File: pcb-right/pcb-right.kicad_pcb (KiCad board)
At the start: 2 copper layers, 84 parts, among them SW1 SW_Push, U1 ATmega32U4-AU, Y1 16MHz

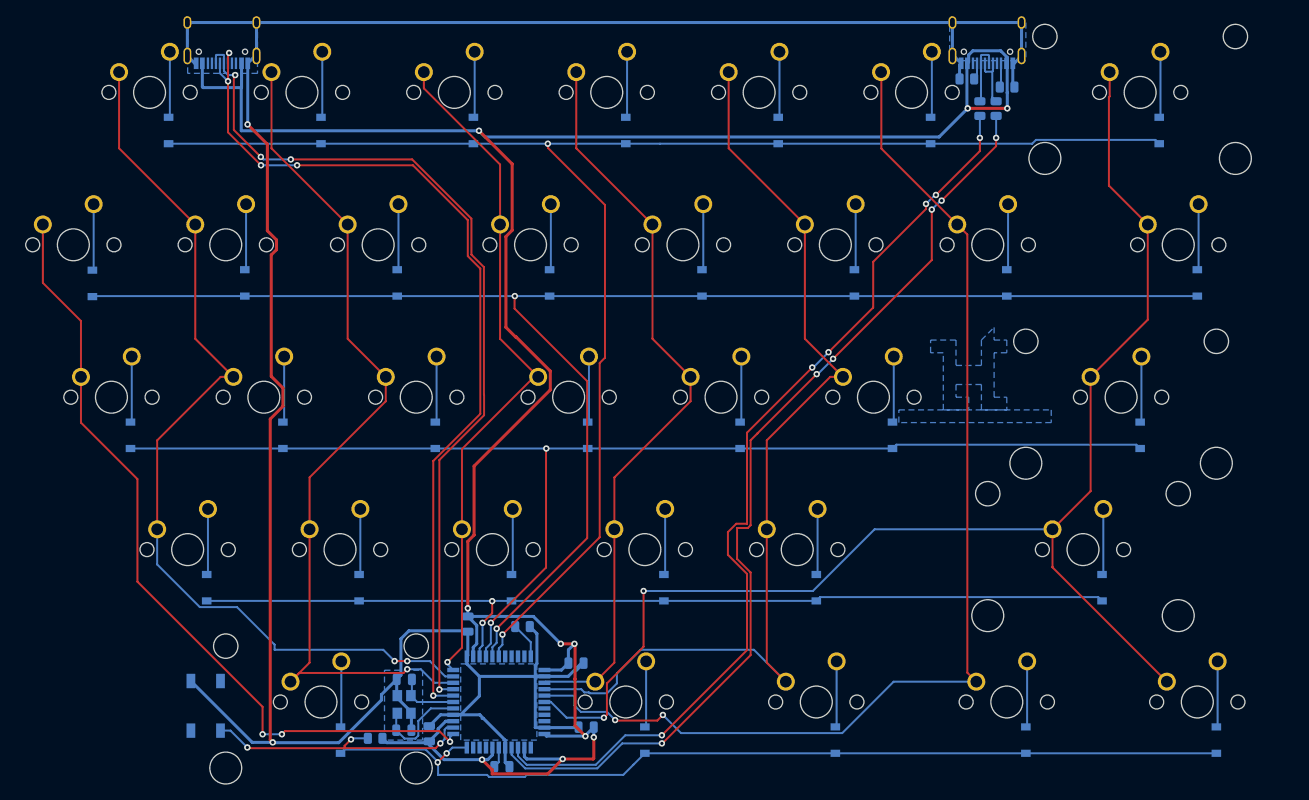
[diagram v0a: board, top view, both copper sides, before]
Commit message: added files for manufacturing right side pcb
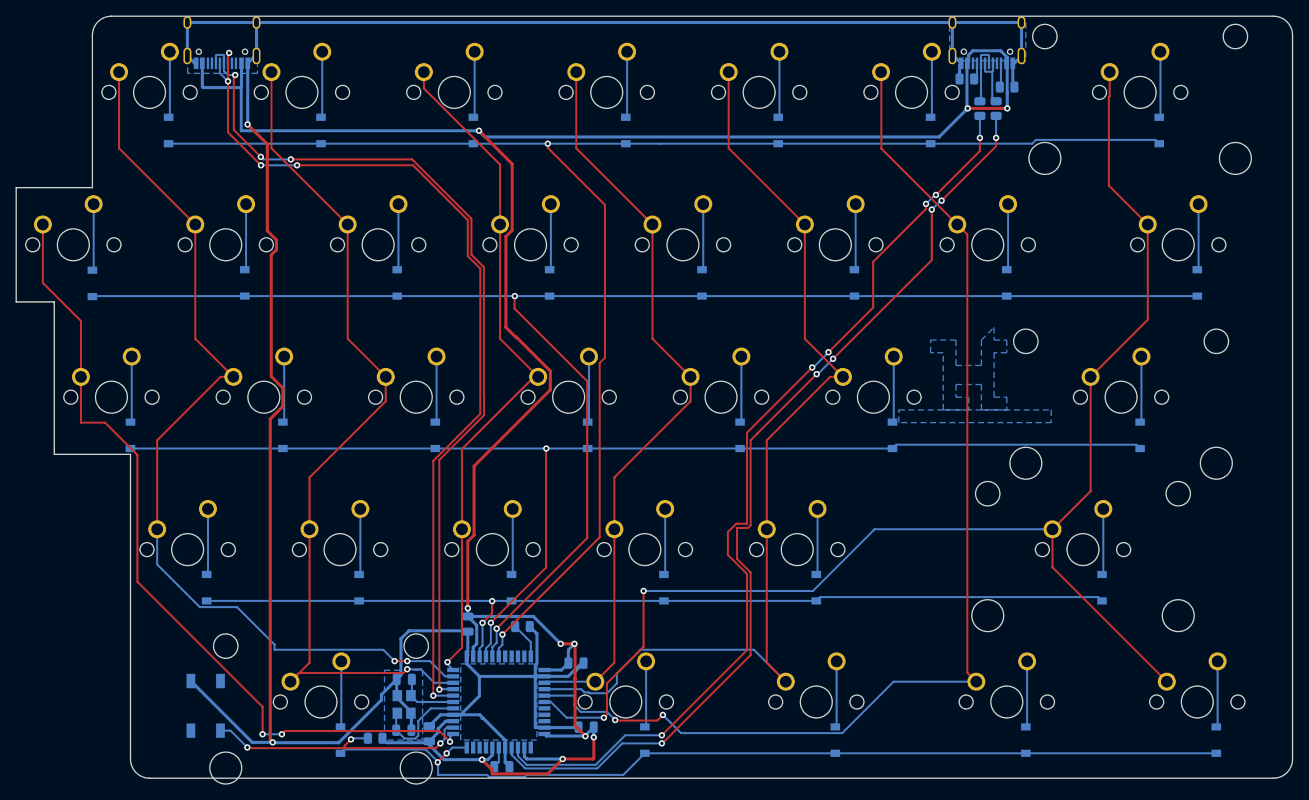
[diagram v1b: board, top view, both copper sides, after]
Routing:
- net col0: track 100.4 -> 102.1 mm
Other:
- board outline added: 159.5 x 95.2 mm

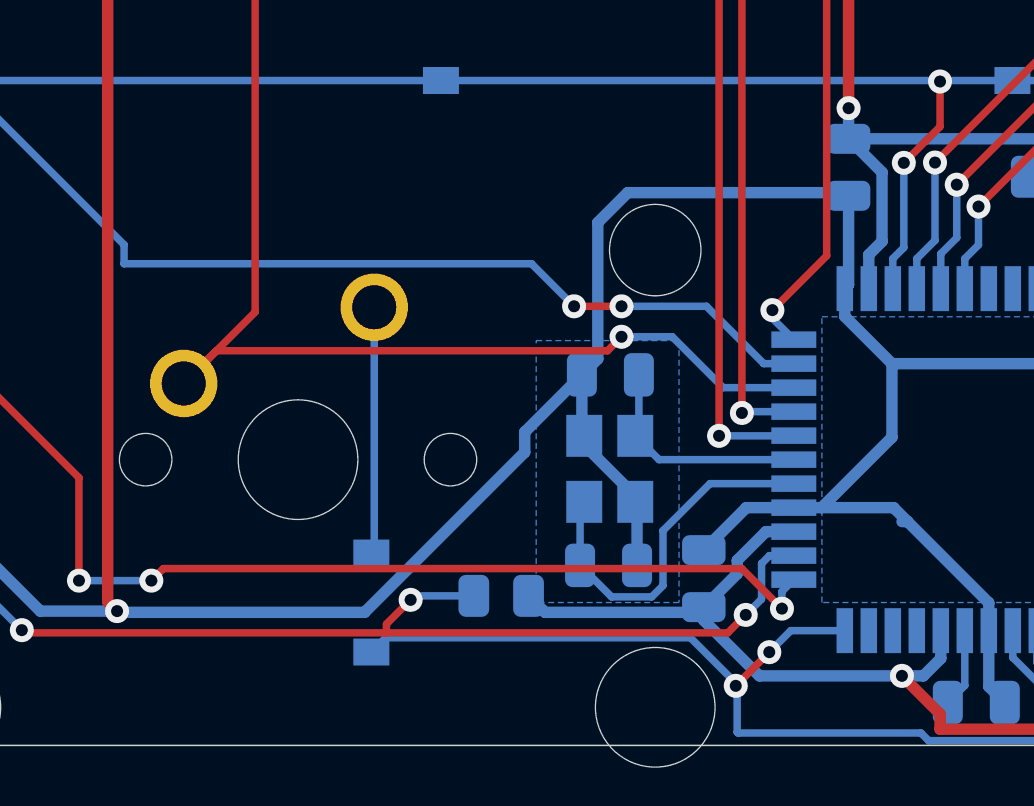
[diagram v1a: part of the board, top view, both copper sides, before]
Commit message: re-zoned crystal area
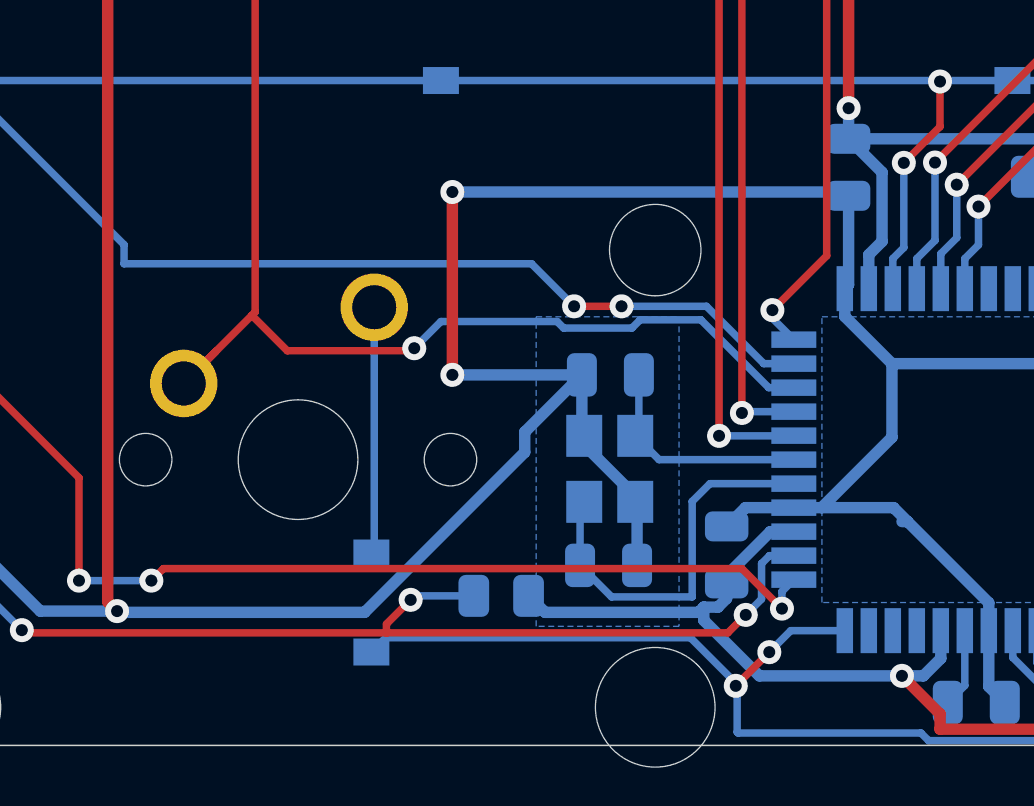
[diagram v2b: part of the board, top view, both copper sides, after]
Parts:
- moved C3 1.10 mm to (73.0, 105.6)
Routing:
- net GND: track 337.0 -> 345.6 mm, vias 2 -> 4
- net Net-(C6-Pad1): track 12.4 -> 13.2 mm
